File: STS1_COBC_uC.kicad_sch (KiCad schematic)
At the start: 40 parts, among them J16 SWD, U18 STWD100PYW83F, U19 STM32F411RET6TR, U28 MCP130T-300I_TT, U29 74LVC1G08GV,125, Y1 12M

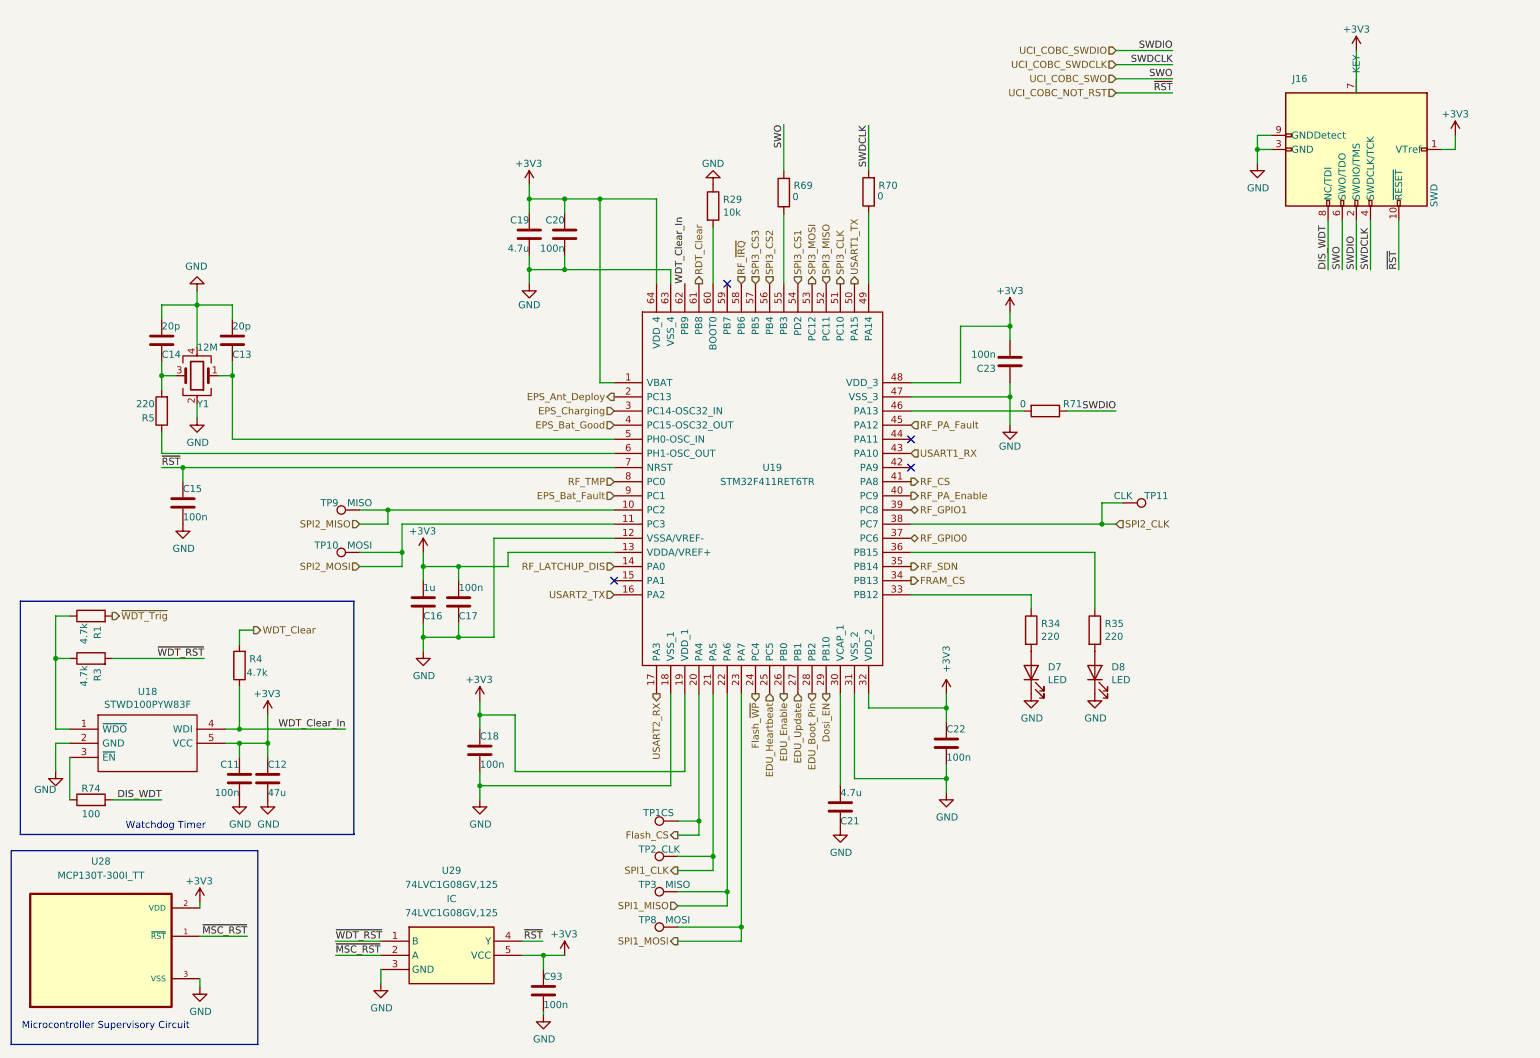
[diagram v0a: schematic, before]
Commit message: Add some redundancy to trigger the RTD: two STM pins should come high for the trigger event to happen
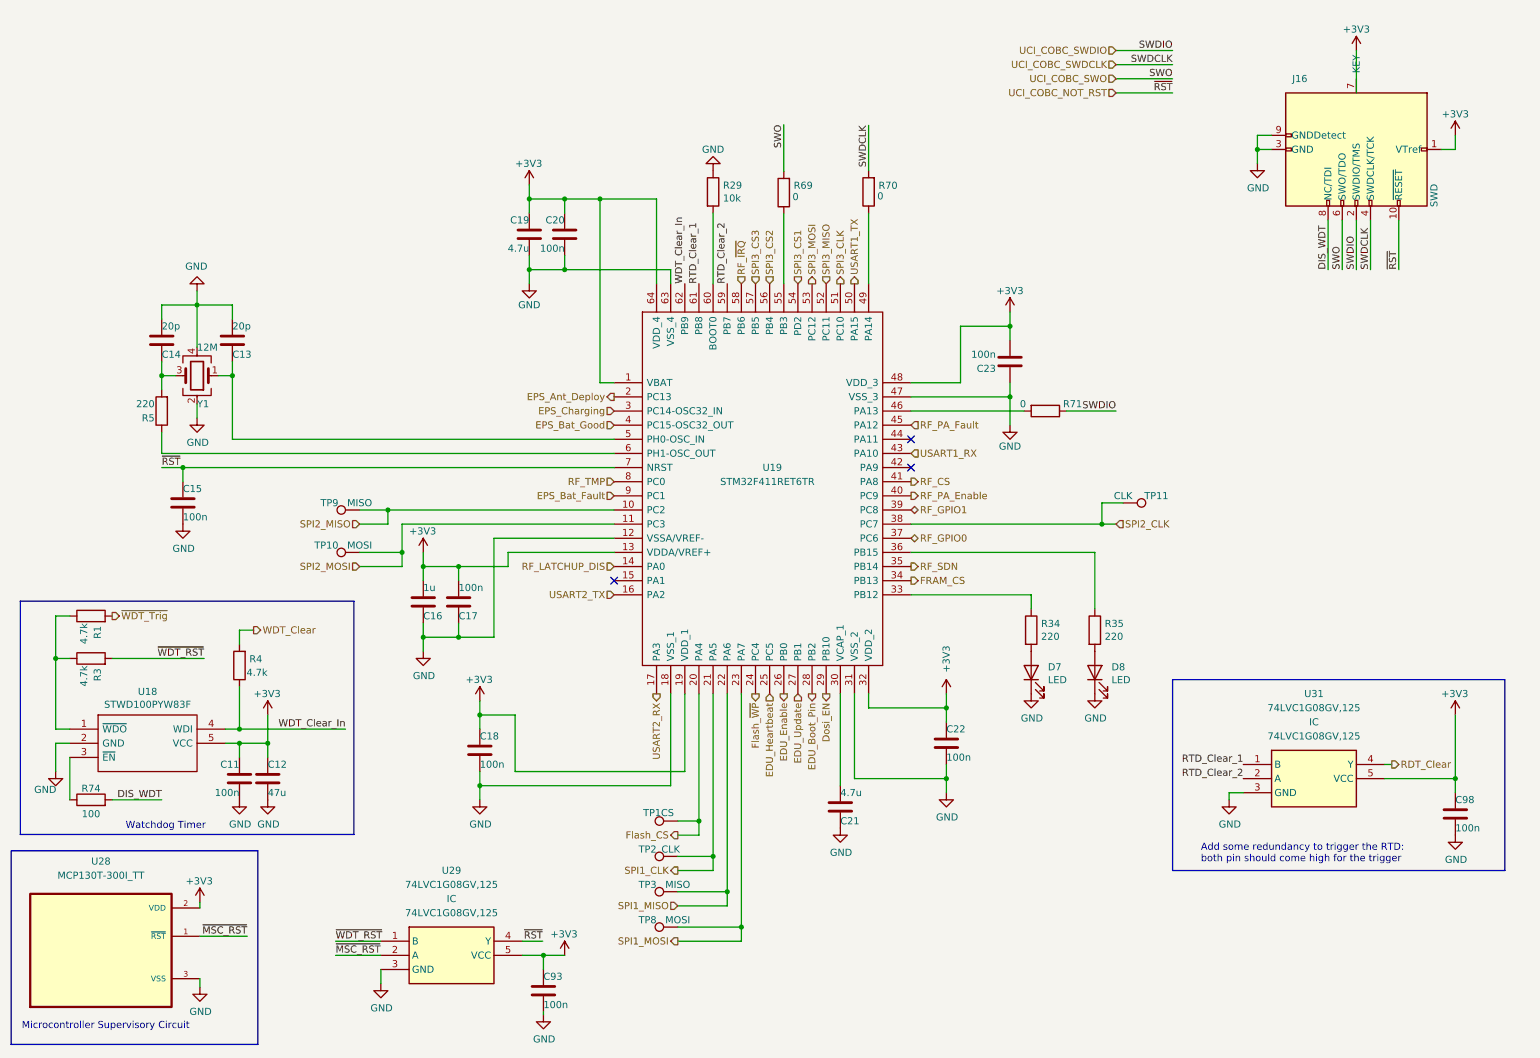
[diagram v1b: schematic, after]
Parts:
- added C98: 100n, Capacitor_SMD:C_0603_1608Metric, symbol Device:C
- added U31: 74LVC1G08GV,125, STSLib:SOT95P275X110-5N, symbol STS1_COBC_V2-rescue:74LVC1G08GV,125
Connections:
- net +3V3: now also C98.2, U31.5 (VCC)
- net GND: now also C98.1, U31.3 (GND)
- net RDT_Clear: now also U31.4 (Y); no longer U19.61 (PB8)
- net RTD_Clear_2: now reaches U19.59 (PB7)
- net RTD_Clear_2: now also U31.2 (A)
- new net RTD_Clear_1: U19.61 (PB8), U31.1 (B)
- no-connect marks 4 -> 3
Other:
- note added: "Add some redundancy to trigger the RTD: both pin should come high for the trigger"
- moved on the sheet: R29

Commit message: Add some redundancy when the latch-up protection of the RF part is disabled: out of two STM pins, at least one should be high
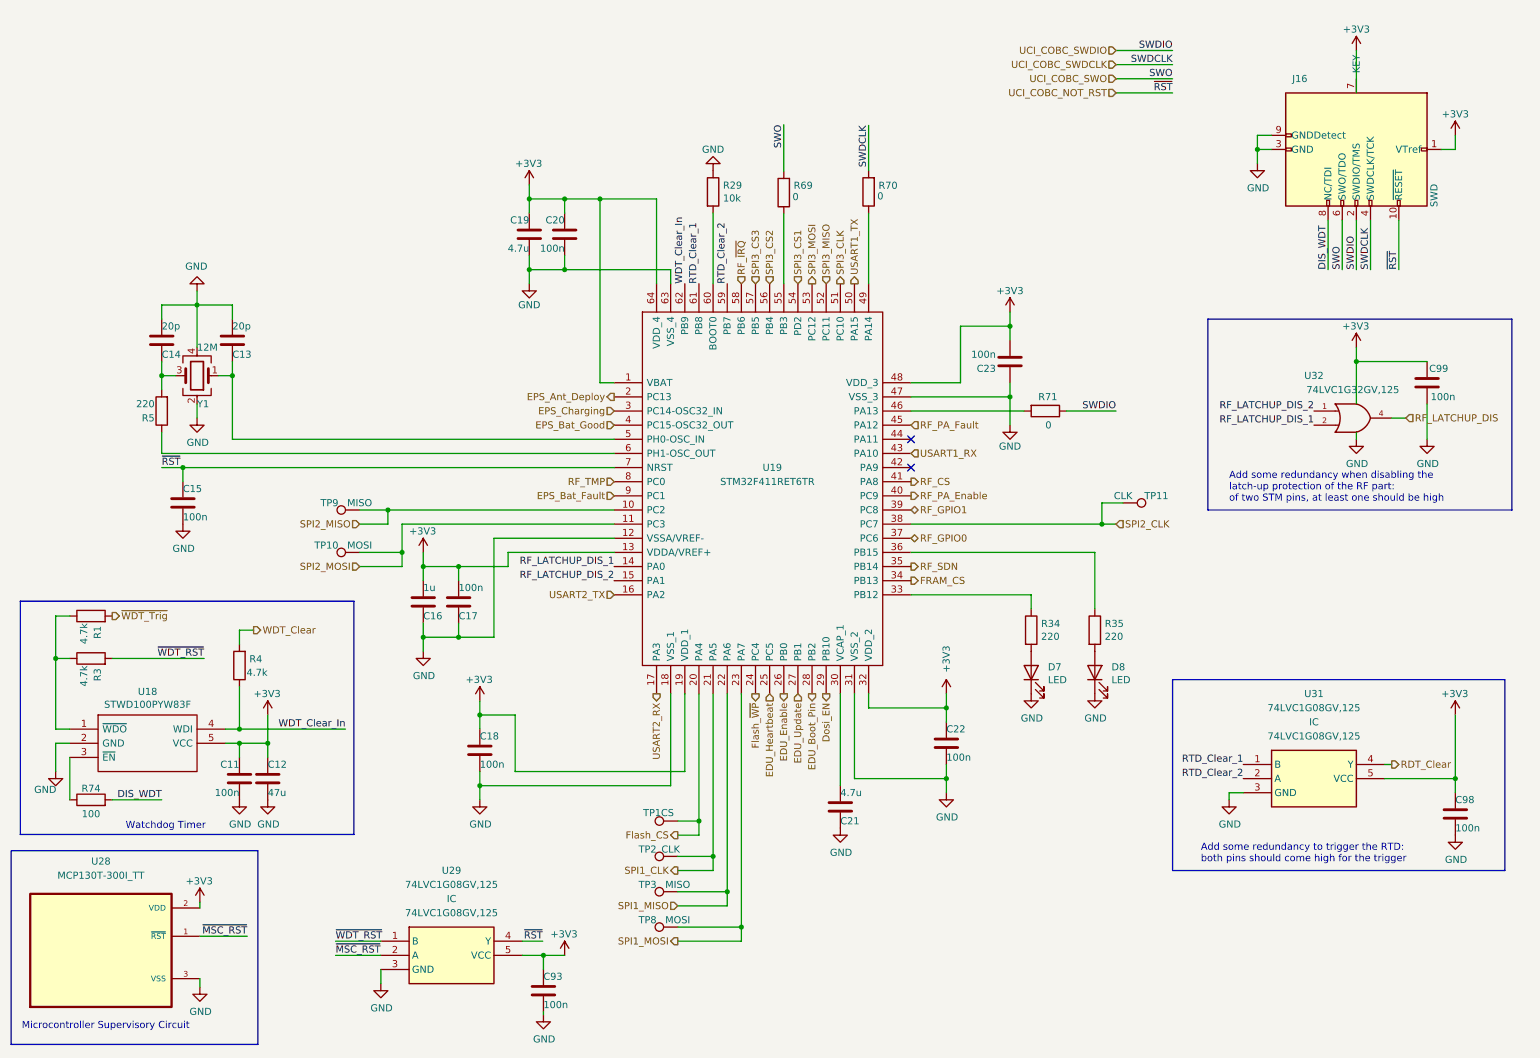
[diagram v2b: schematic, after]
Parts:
- added C99: 100n, Capacitor_SMD:C_0603_1608Metric, symbol Device:C
- added U32: 74LVC1G32GV,125, STSLib:SOT95P275X110-5N, symbol 74xGxx:74LVC1G32
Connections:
- net +3V3: now also C99.1, U32.5 (VCC)
- net GND: now also C99.2, U32.3 (GND)
- net RF_LATCHUP_DIS: now also U32.4; no longer U19.14 (PA0)
- net RF_LATCHUP_DIS_2: now reaches U19.15 (PA1)
- net RF_LATCHUP_DIS_2: now also U32.1
- new net RF_LATCHUP_DIS_1: U19.14 (PA0), U32.2
- no-connect marks 3 -> 2
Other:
- note added: "Add some redundancy to trigger the RTD: both pins should come high for the trigger"
- note added: "Add some redundancy when disabling the latch-up protection of the RF part: of two STM pins, at least one should be high"
- note removed: "Add some redundancy to trigger the RTD: both pin should come high for the trigger"
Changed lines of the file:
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@@
   (junction (at 44.45 92.71) (diameter 0) (color 0 0 0 0)
+  )
+  (junction (at 255.27 73.66) (diameter 0) (color 0 0 0 0)
   )
   (junction (at 54.61 142.24) (diameter 0) (color 0 0 0 0)
@@
   (no_connect (at 175.26 92.71))
   (no_connect (at 175.26 87.63))
-  (no_connect (at 121.92 113.03))
   (wire (pts (xy 53.34 63.5) (xy 46.99 63.5))
     (stroke (width 0) (type default) (color 0 0 0 0))
@@
     (stroke (width 0) (type default) (color 0 0 0 0))
   )
+  (polyline (pts (xy 283.21 100.33) (xy 283.21 66.04))
+    (stroke (width 0) (type default) (color 0 0 0 0))
+  )
   (wire (pts (xy 113.03 44.45) (xy 113.03 46.99))
     (stroke (width 0) (type default) (color 0 0 0 0))
@@
     (stroke (width 0) (type default) (color 0 0 0 0))
   )
+  (wire (pts (xy 255.27 71.12) (xy 255.27 73.66))
+    (stroke (width 0) (type default) (color 0 0 0 0))
+  )
   (polyline (pts (xy 57.912 196.342) (xy 57.912 161.544))
     (stroke (width 0) (type default) (color 0 0 0 0))
@@
     (stroke (width 0) (type default) (color 0 0 0 0))
   )
+  (wire (pts (xy 255.27 73.66) (xy 267.97 73.66))
+    (stroke (width 0) (type default) (color 0 0 0 0))
+  )
   (wire (pts (xy 167.64 46.99) (xy 167.64 59.69))
     (stroke (width 0) (type default) (color 0 0 0 0))
@@
     (stroke (width 0) (type default) (color 0 0 0 0))
   )
+  (wire (pts (xy 255.27 86.36) (xy 255.27 87.63))
+    (stroke (width 0) (type default) (color 0 0 0 0))
+  )
   (wire (pts (xy 53.34 66.04) (xy 53.34 63.5))
     (stroke (width 0) (type default) (color 0 0 0 0))
@@
     (stroke (width 0) (type default) (color 0 0 0 0))
   )
+  (wire (pts (xy 255.27 73.66) (xy 255.27 81.28))
+    (stroke (width 0) (type default) (color 0 0 0 0))
+  )
   (polyline (pts (xy 222.25 130.81) (xy 281.94 130.81))
     (stroke (width 0) (type default) (color 0 0 0 0))
@@
     (stroke (width 0) (type default) (color 0 0 0 0))
   )
+  (polyline (pts (xy 228.6 66.04) (xy 228.6 100.33))
+    (stroke (width 0) (type default) (color 0 0 0 0))
+  )
   (wire (pts (xy 209.55 102.87) (xy 212.09 102.87))
     (stroke (width 0) (type default) (color 0 0 0 0))
@@
     (stroke (width 0) (type default) (color 0 0 0 0))
   )
+  (wire (pts (xy 267.97 81.28) (xy 267.97 87.63))
+    (stroke (width 0) (type default) (color 0 0 0 0))
+  )
   (wire (pts (xy 40.64 90.17) (xy 40.64 86.36))
     (stroke (width 0) (type default) (color 0 0 0 0))
@@
     (stroke (width 0) (type default) (color 0 0 0 0))
   )
+  (wire (pts (xy 261.62 83.82) (xy 264.16 83.82))
+    (stroke (width 0) (type default) (color 0 0 0 0))
+  )
   (wire (pts (xy 105.41 177.8) (xy 109.093 177.8))
     (stroke (width 0) (type default) (color 0 0 0 0))
@@
     (stroke (width 0) (type default) (color 0 0 0 0))
   )
+  (polyline (pts (xy 228.6 100.33) (xy 283.21 100.33))
+    (stroke (width 0) (type default) (color 0 0 0 0))
+  )
   (wire (pts (xy 102.87 107.95) (xy 102.87 110.49))
     (stroke (width 0) (type default) (color 0 0 0 0))
@@
     (stroke (width 0) (type default) (color 0 0 0 0))
   )
+  (polyline (pts (xy 228.6 66.04) (xy 283.21 66.04))
+    (stroke (width 0) (type default) (color 0 0 0 0))
+  )
   (wire (pts (xy 133.35 156.21) (xy 137.16 156.21))
     (stroke (width 0) (type default) (color 0 0 0 0))
@@
     (stroke (width 0) (type default) (color 0 0 0 0))
   )
-  (text "Add some redundancy to trigger the RTD:\nboth pin should come high for the trigger"
+  (text "Add some redundancy to trigger the RTD:\nboth pins should come high for the trigger"
     (at 227.33 163.83 0)
     (effects (font (size 1.27 1.27)) (justify left bottom))
@@
     (effects (font (size 1.27 1.27)) (justify left bottom))
   )
+  (text "Add some redundancy when disabling the\nlatch-up protection of the RF part:\nof two STM pins, at least one should be high"
+    (at 232.41 99.06 0)
+    (effects (font (size 1.27 1.27)) (justify left bottom))
+  )
   (text "Watchdog Timer" (at 34.163 157.861 0)
     (effects (font (size 1.27 1.27)) (justify left bottom))
@@
     (effects (font (size 1.27 1.27)) (justify right bottom))
   )
+  (label "RF_LATCHUP_DIS_2" (at 121.92 113.03 180)
+    (effects (font (size 1.27 1.27)) (justify right bottom))
+  )
   (label "~{RST}" (at 222.25 25.4 180)
     (effects (font (size 1.27 1.27)) (justify right bottom))
@@
     (effects (font (size 1.27 1.27)) (justify left bottom))
   )
+  (label "RF_LATCHUP_DIS_1" (at 121.92 110.49 180)
+    (effects (font (size 1.27 1.27)) (justify right bottom))
+  )
   (label "DIS_WDT" (at 250.19 57.15 90)
     (effects (font (size 1.27 1.27)) (justify left bottom))
@@
     (effects (font (size 1.27 1.27)) (justify right bottom))
   )
+  (label "RF_LATCHUP_DIS_1" (at 247.65 85.09 180)
+    (effects (font (size 1.27 1.27)) (justify right bottom))
+  )
   (label "RTD_Clear_2" (at 234.95 148.59 180)
     (effects (font (size 1.27 1.27)) (justify right bottom))
   )
+  (label "RF_LATCHUP_DIS_2" (at 247.65 82.55 180)
+    (effects (font (size 1.27 1.27)) (justify right bottom))
+  )
   (label "RTD_Clear_1" (at 137.16 59.69 90)
     (effects (font (size 1.27 1.27)) (justify left bottom))
@@
     (effects (font (size 1.27 1.27)) (justify right))
   )
-  (hierarchical_label "RF_LATCHUP_DIS" (shape input) (at 121.92 110.49 180)
-    (effects (font (size 1.27 1.27)) (justify right))
+  (hierarchical_label "RF_LATCHUP_DIS" (shape input) (at 264.16 83.82 0)
+    (effects (font (size 1.27 1.27)) (justify left))
   )
   (hierarchical_label "SPI2_MOSI" (shape input) (at 76.2 110.49 180)
@@
     (pin "4")
   )
+  (symbol (lib_id "power:GND") (at 255.27 87.63 0) (unit 1)
+    (in_bom yes) (on_board yes)
+    (property "Reference" "#PWR067" (id 0) (at 255.27 93.98 0)
+      (effects (font (size 1.27 1.27)) hide)
+    )
+    (property "Value" "GND" (id 1) (at 255.397 92.0242 0))
+    (property "Footprint" "" (id 2) (at 255.27 87.63 0)
+      (effects (font (size 1.27 1.27)) hide)
+    )
+    (property "Datasheet" "" (id 3) (at 255.27 87.63 0)
+      (effects (font (size 1.27 1.27)) hide)
+    )
+    (pin "1")
+  )
+  (symbol (lib_id "power:GND") (at 267.97 87.63 0) (unit 1)
+    (in_bom yes) (on_board yes)
+    (property "Reference" "#PWR070" (id 0) (at 267.97 93.98 0)
+      (effects (font (size 1.27 1.27)) hide)
+    )
+    (property "Value" "GND" (id 1) (at 268.097 92.0242 0))
+    (property "Footprint" "" (id 2) (at 267.97 87.63 0)
+      (effects (font (size 1.27 1.27)) hide)
+    )
+    (property "Datasheet" "" (id 3) (at 267.97 87.63 0)
+      (effects (font (size 1.27 1.27)) hide)
+    )
+    (pin "1")
+  )
   (symbol (lib_id "Connector:TestPoint") (at 133.35 175.26 90) (unit 1)
     (in_bom no) (on_board yes)
@@
     (pin "4")
     (pin "5")
+  )
+  (symbol (lib_id "power:+3V3") (at 255.27 71.12 0) (unit 1)
+    (in_bom yes) (on_board yes)
+    (property "Reference" "#PWR065" (id 0) (at 255.27 74.93 0)
+      (effects (font (size 1.27 1.27)) hide)
+    )
+    (property "Value" "+3V3" (id 1) (at 252.73 67.31 0)
+      (effects (font (size 1.27 1.27)) (justify left))
+    )
+    (property "Footprint" "" (id 2) (at 255.27 71.12 0)
+      (effects (font (size 1.27 1.27)) hide)
+    )
+    (property "Datasheet" "" (id 3) (at 255.27 71.12 0)
+      (effects (font (size 1.27 1.27)) hide)
+    )
+    (pin "1")
   )
   (symbol (lib_id "power:GND") (at 196.85 133.35 0) (unit 1)
@@
     (pin "3")
   )
+  (symbol (lib_id "74xGxx:74LVC1G32") (at 255.27 83.82 0) (unit 1)
+    (in_bom yes) (on_board yes)
+    (property "Reference" "U32" (id 0) (at 247.65 76.2 0))
+    (property "Value" "74LVC1G32GV,125 " (id 1) (at 254.635 78.74 0))
+    (property "Footprint" "STSLib:SOT95P275X110-5N" (id 2) (at 255.27 83.82 0)
+      (effects (font (size 1.27 1.27)) hide)
+    )
+    (property "Datasheet" "http://www.ti.com/lit/sg/scyt129e/scyt129e.pdf" (id 3) (at 255.27 83.82 0)
+      (effects (font (size 1.27 1.27)) hide)
+    )
+    (property "JLCPCB Part #" "C12517" (id 4) (at 255.27 83.82 0)
+      (effects (font (size 1.27 1.27)) hide)
+    )
+    (property "Manufacturer_Part_Number" "74LVC1G32GV,125 " (id 5) (at 255.27 83.82 0)
+      (effects (font (size 1.27 1.27)) hide)
+    )
+    (pin "1")
+    (pin "2")
+    (pin "3")
+    (pin "4")
+    (pin "5")
+  )
   (symbol (lib_id "power:+3V3") (at 97.79 134.62 0) (unit 1)
     (in_bom yes) (on_board yes)
@@
   (symbol (lib_id "Device:R") (at 199.39 82.55 270) (unit 1)
     (in_bom yes) (on_board yes)
-    (property "Reference" "R71" (id 0) (at 202.565 81.28 90)
-      (effects (font (size 1.27 1.27)) (justify left))
-    )
-    (property "Value" "0" (id 1) (at 194.818 81.28 90)
+    (property "Reference" "R71" (id 0) (at 198.12 80.01 90)
+      (effects (font (size 1.27 1.27)) (justify left))
+    )
+    (property "Value" "0" (id 1) (at 199.39 85.09 90)
       (effects (font (size 1.27 1.27)) (justify left))
     )
@@
     (pin "1")
   )
+  (symbol (lib_id "Device:C") (at 267.97 77.47 0) (unit 1)
+    (in_bom yes) (on_board yes)
+    (property "Reference" "C99" (id 0) (at 271.78 74.93 0)
+      (effects (font (size 1.27 1.27)) (justify right))
+    )
+    (property "Value" "100n" (id 1) (at 273.05 80.01 0)
+      (effects (font (size 1.27 1.27)) (justify right))
+    )
+    (property "Footprint" "Capacitor_SMD:C_0603_1608Metric" (id 2) (at 268.9352 81.28 0)
+      (effects (font (size 1.27 1.27)) hide)
+    )
+    (property "Datasheet" "~" (id 3) (at 267.97 77.47 0)
+      (effects (font (size 1.27 1.27)) hide)
+    )
+    (property "JLCPCB Part #" "C1591" (id 4) (at 267.97 77.47 0)
+      (effects (font (size 1.27 1.27)) hide)
+    )
+    (property "Manufacturer_Part_Number" "CL10B104KB8NNNC " (id 5) (at 267.97 77.47 0)
+      (effects (font (size 1.27 1.27)) hide)
+    )
+    (pin "1")
+    (pin "2")
+  )
   (symbol (lib_id "power:GND") (at 273.05 158.75 0) (unit 1)
